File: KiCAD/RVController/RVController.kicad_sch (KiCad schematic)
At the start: 67 parts, among them IC1 MCP2561FD-E/P, J1 1727078, J2 1727078, J3 1727078, J4 1727078, J5 4-1437652-0, J6 Conn_01x02_Male, J7 Conn_01x02_Male, J8 54602-908LF, J9 54602-908LF, U1 FREESOC_MINI, U2 74HCT541, U3 VX7805-500, U4 H11L1SR2M, U5 H11L1SR2M, Y1 ECS-3961-240-AU-TR

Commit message: Almost done
Added mounting holes, labels, etc.
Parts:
- added H1, H2, H3, H4, H5, H6, H7, H8: MountingHole, MountingHole:MountingHole_3.2mm_M3_ISO14580, symbol Mechanical:MountingHole
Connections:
- net CAN_RX: now also U1.29 (15.5)
- net CAN_TX: now also U1.30 (15.4)
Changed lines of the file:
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@@
     (stroke (width 0) (type default) (color 0 0 0 0))
   )
+  (wire (pts (xy 66.04 68.58) (xy 77.47 68.58))
+    (stroke (width 0) (type default) (color 0 0 0 0))
+  )
   (wire (pts (xy 389.89 151.13) (xy 393.7 151.13))
     (stroke (width 0) (type default) (color 0 0 0 0))
@@
     (stroke (width 0) (type default) (color 0 0 0 0))
   )
+  (wire (pts (xy 66.04 71.12) (xy 77.47 71.12))
+    (stroke (width 0) (type default) (color 0 0 0 0))
+  )
   (wire (pts (xy 133.35 157.48) (xy 142.24 157.48))
     (stroke (width 0) (type default) (color 0 0 0 0))
@@
     (effects (font (size 1.27 1.27)) (justify left bottom))
   )
+  (label "CAN_RX" (at 77.47 71.12 0)
+    (effects (font (size 1.27 1.27)) (justify left bottom))
+  )
+  (label "CAN_TX" (at 77.47 68.58 0)
+    (effects (font (size 1.27 1.27)) (justify left bottom))
+  )
   (label "CAN_TX" (at 157.48 226.06 0)
     (effects (font (size 1.27 1.27)) (justify left bottom))
@@
     (pin "1")
   )
+  (symbol (lib_id "Mechanical:MountingHole") (at 335.28 250.19 0) (unit 1)
+    (in_bom no) (on_board yes) (fields_autoplaced)
+    (property "Reference" "H8" (id 0) (at 337.82 248.9199 0)
+      (effects (font (size 1.27 1.27)) (justify left))
+    )
+    (property "Value" "MountingHole" (id 1) (at 337.82 251.4599 0)
+      (effects (font (size 1.27 1.27)) (justify left))
+    )
+    (property "Footprint" "MountingHole:MountingHole_3.2mm_M3_ISO14580" (id 2) (at 335.28 250.19 0)
+      (effects (font (size 1.27 1.27)) hide)
+    )
+    (property "Datasheet" "~" (id 3) (at 335.28 250.19 0)
+      (effects (font (size 1.27 1.27)) hide)
+    )
+  )
   (symbol (lib_id "Device:R") (at 125.73 123.19 90) (unit 1)
     (in_bom yes) (on_board yes)
@@
     (pin "2")
   )
+  (symbol (lib_id "Mechanical:MountingHole") (at 335.28 240.03 0) (unit 1)
+    (in_bom no) (on_board yes) (fields_autoplaced)
+    (property "Reference" "H6" (id 0) (at 337.82 238.7599 0)
+      (effects (font (size 1.27 1.27)) (justify left))
+    )
+    (property "Value" "MountingHole" (id 1) (at 337.82 241.2999 0)
+      (effects (font (size 1.27 1.27)) (justify left))
+    )
+    (property "Footprint" "MountingHole:MountingHole_3.2mm_M3_ISO14580" (id 2) (at 335.28 240.03 0)
+      (effects (font (size 1.27 1.27)) hide)
+    )
+    (property "Datasheet" "~" (id 3) (at 335.28 240.03 0)
+      (effects (font (size 1.27 1.27)) hide)
+    )
+  )
   (symbol (lib_id "power:+5V_CAN") (at 210.82 207.01 0) (unit 1)
     (in_bom yes) (on_board yes) (fields_autoplaced)
@@
     (pin "2")
   )
+  (symbol (lib_id "Mechanical:MountingHole") (at 335.28 245.11 0) (unit 1)
+    (in_bom no) (on_board yes) (fields_autoplaced)
+    (property "Reference" "H7" (id 0) (at 337.82 243.8399 0)
+      (effects (font (size 1.27 1.27)) (justify left))
+    )
+    (property "Value" "MountingHole" (id 1) (at 337.82 246.3799 0)
+      (effects (font (size 1.27 1.27)) (justify left))
+    )
+    (property "Footprint" "MountingHole:MountingHole_3.2mm_M3_ISO14580" (id 2) (at 335.28 245.11 0)
+      (effects (font (size 1.27 1.27)) hide)
+    )
+    (property "Datasheet" "~" (id 3) (at 335.28 245.11 0)
+      (effects (font (size 1.27 1.27)) hide)
+    )
+  )
   (symbol (lib_id "Device:R") (at 59.69 153.67 0) (unit 1)
     (in_bom yes) (on_board yes)
@@
     (pin "C")
   )
+  (symbol (lib_id "Mechanical:MountingHole") (at 335.28 234.95 0) (unit 1)
+    (in_bom no) (on_board yes) (fields_autoplaced)
+    (property "Reference" "H5" (id 0) (at 337.82 233.6799 0)
+      (effects (font (size 1.27 1.27)) (justify left))
+    )
+    (property "Value" "MountingHole" (id 1) (at 337.82 236.2199 0)
+      (effects (font (size 1.27 1.27)) (justify left))
+    )
+    (property "Footprint" "MountingHole:MountingHole_3.2mm_M3_ISO14580" (id 2) (at 335.28 234.95 0)
+      (effects (font (size 1.27 1.27)) hide)
+    )
+    (property "Datasheet" "~" (id 3) (at 335.28 234.95 0)
+      (effects (font (size 1.27 1.27)) hide)
+    )
+  )
   (symbol (lib_id "power:GND") (at 33.02 91.44 0) (unit 1)
     (in_bom yes) (on_board yes) (fields_autoplaced)
@@
     (pin "C")
   )
+  (symbol (lib_id "Mechanical:MountingHole") (at 335.28 229.87 0) (unit 1)
+    (in_bom no) (on_board yes) (fields_autoplaced)
+    (property "Reference" "H4" (id 0) (at 337.82 228.5999 0)
+      (effects (font (size 1.27 1.27)) (justify left))
+    )
+    (property "Value" "MountingHole" (id 1) (at 337.82 231.1399 0)
+      (effects (font (size 1.27 1.27)) (justify left))
+    )
+    (property "Footprint" "MountingHole:MountingHole_3.2mm_M3_ISO14580" (id 2) (at 335.28 229.87 0)
+      (effects (font (size 1.27 1.27)) hide)
+    )
+    (property "Datasheet" "~" (id 3) (at 335.28 229.87 0)
+      (effects (font (size 1.27 1.27)) hide)
+    )
+  )
   (symbol (lib_id "Device:R") (at 59.69 186.69 0) (unit 1)
     (in_bom yes) (on_board yes)
@@
     (pin "1")
   )
+  (symbol (lib_id "Mechanical:MountingHole") (at 335.28 214.63 0) (unit 1)
+    (in_bom no) (on_board yes) (fields_autoplaced)
+    (property "Reference" "H1" (id 0) (at 337.82 213.3599 0)
+      (effects (font (size 1.27 1.27)) (justify left))
+    )
+    (property "Value" "MountingHole" (id 1) (at 337.82 215.8999 0)
+      (effects (font (size 1.27 1.27)) (justify left))
+    )
+    (property "Footprint" "MountingHole:MountingHole_3.2mm_M3_ISO14580" (id 2) (at 335.28 214.63 0)
+      (effects (font (size 1.27 1.27)) hide)
+    )
+    (property "Datasheet" "~" (id 3) (at 335.28 214.63 0)
+      (effects (font (size 1.27 1.27)) hide)
+    )
+  )
   (symbol (lib_id "power:+5V") (at 66.04 43.18 0) (unit 1)
     (in_bom yes) (on_board yes) (fields_autoplaced)
@@
     (pin "1")
   )
+  (symbol (lib_id "Mechanical:MountingHole") (at 335.28 219.71 0) (unit 1)
+    (in_bom no) (on_board yes) (fields_autoplaced)
+    (property "Reference" "H2" (id 0) (at 337.82 218.4399 0)
+      (effects (font (size 1.27 1.27)) (justify left))
+    )
+    (property "Value" "MountingHole" (id 1) (at 337.82 220.9799 0)
+      (effects (font (size 1.27 1.27)) (justify left))
+    )
+    (property "Footprint" "MountingHole:MountingHole_3.2mm_M3_ISO14580" (id 2) (at 335.28 219.71 0)
+      (effects (font (size 1.27 1.27)) hide)
+    )
+    (property "Datasheet" "~" (id 3) (at 335.28 219.71 0)
+      (effects (font (size 1.27 1.27)) hide)
+    )
+  )
   (symbol (lib_id "power:GND_CAN") (at 218.44 271.78 0) (unit 1)
     (in_bom yes) (on_board yes) (fields_autoplaced)
@@
     (pin "1")
   )
+  (symbol (lib_id "Mechanical:MountingHole") (at 335.28 224.79 0) (unit 1)
+    (in_bom no) (on_board yes) (fields_autoplaced)
+    (property "Reference" "H3" (id 0) (at 337.82 223.5199 0)
+      (effects (font (size 1.27 1.27)) (justify left))
+    )
+    (property "Value" "MountingHole" (id 1) (at 337.82 226.0599 0)
+      (effects (font (size 1.27 1.27)) (justify left))
+    )
+    (property "Footprint" "MountingHole:MountingHole_3.2mm_M3_ISO14580" (id 2) (at 335.28 224.79 0)
+      (effects (font (size 1.27 1.27)) hide)
+    )
+    (property "Datasheet" "~" (id 3) (at 335.28 224.79 0)
+      (effects (font (size 1.27 1.27)) hide)
+    )
+  )
   (symbol (lib_id "Schematic:SS16MH") (at 247.65 110.49 90) (unit 1)
     (in_bom yes) (on_board yes) (fields_autoplaced)
@@
       (reference "D26") (unit 1) (value "ATV02W240B") (footprint "Footprints:SODFL2512X73N")
     )
+    (path "/c704bbfb-71ae-4908-a3cf-bc2bd43df023"
+      (reference "H1") (unit 1) (value "MountingHole") (footprint "MountingHole:MountingHole_3.2mm_M3_ISO14580")
+    )
+    (path "/de77b565-8d7d-4e6e-8ab1-bcd72032f282"
+      (reference "H2") (unit 1) (value "MountingHole") (footprint "MountingHole:MountingHole_3.2mm_M3_ISO14580")
+    )
+    (path "/e980f142-5464-462f-987b-1671d88515a0"
+      (reference "H3") (unit 1) (value "MountingHole") (footprint "MountingHole:MountingHole_3.2mm_M3_ISO14580")
+    )
+    (path "/bfa32192-5b21-496a-9b92-6fdd025d263e"
+      (reference "H4") (unit 1) (value "MountingHole") (footprint "MountingHole:MountingHole_3.2mm_M3_ISO14580")
+    )
+    (path "/684fccac-62c3-4aa7-b45b-93649e0e524d"
+      (reference "H5") (unit 1) (value "MountingHole") (footprint "MountingHole:MountingHole_3.2mm_M3_ISO14580")
+    )
+    (path "/55708a54-043a-40dd-a394-e39898b05970"
+      (reference "H6") (unit 1) (value "MountingHole") (footprint "MountingHole:MountingHole_3.2mm_M3_ISO14580")
+    )
+    (path "/5d658465-34e3-47c9-8c1c-64276b8eda22"
+      (reference "H7") (unit 1) (value "MountingHole") (footprint "MountingHole:MountingHole_3.2mm_M3_ISO14580")
+    )
+    (path "/34b1f6de-8080-4231-916b-2ce7a1c2638e"
+      (reference "H8") (unit 1) (value "MountingHole") (footprint "MountingHole:MountingHole_3.2mm_M3_ISO14580")
+    )
     (path "/dbe415dc-83a6-4820-a16b-1dc1bf799f8a"

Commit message: Done?
Routed, etc. Exported STEP.
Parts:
- removed H8: MountingHole, MountingHole:MountingHole_3.2mm_M3_ISO14580, symbol Mechanical:MountingHole
- added C8: 4700pF, Capacitor_SMD:C_0603_1608Metric, symbol Device:C
- added J10, J11: Conn_01x02_Male, Connector_PinHeader_2.54mm:PinHeader_1x02_P2.54mm_Vertical, symbol Connector:Conn_01x02_Male
- added J12: 284392-2, Footprints:TE_284392-2, symbol Schematic:284392-2
- added R23: 300R, Resistor_SMD:R_0805_2012Metric, symbol Device:R
- added R24, R29: 60R, Resistor_SMD:R_0805_2012Metric, symbol Device:R
- J1, J3, J4: footprint PHOENIX_1727078 -> Footprints:PHOENIX_1727078
- J2: footprint PHOENIX_1727078 -> Footprints:PHOENIX_1727078; PN (none) -> 1727078
- J5: footprint TE_4-1437652-0 -> Footprints:TE_4-1437652-0
- R17, R22: value 330R -> 300R; PN RMCF0805JT330R -> RMCF0805JT300R
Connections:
- net +5V_CAN: now also J12.1
- net CANH: now also J10.1 (Pin_1)
- net CANL: now also J11.1 (Pin_1)
- net at IC1.5 (SPLIT): now also R23.1
- net GNDPWR renamed GND_CAN
- net GND_CAN: now also C8.2, J12.2
- new net: C8.1, R23.2, R24.2, R29.1
- new net: J11.2 (Pin_2), R29.2
- new net: J10.2 (Pin_2), R24.1
- no-connect marks 0 -> 25
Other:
- moved on the sheet: C6

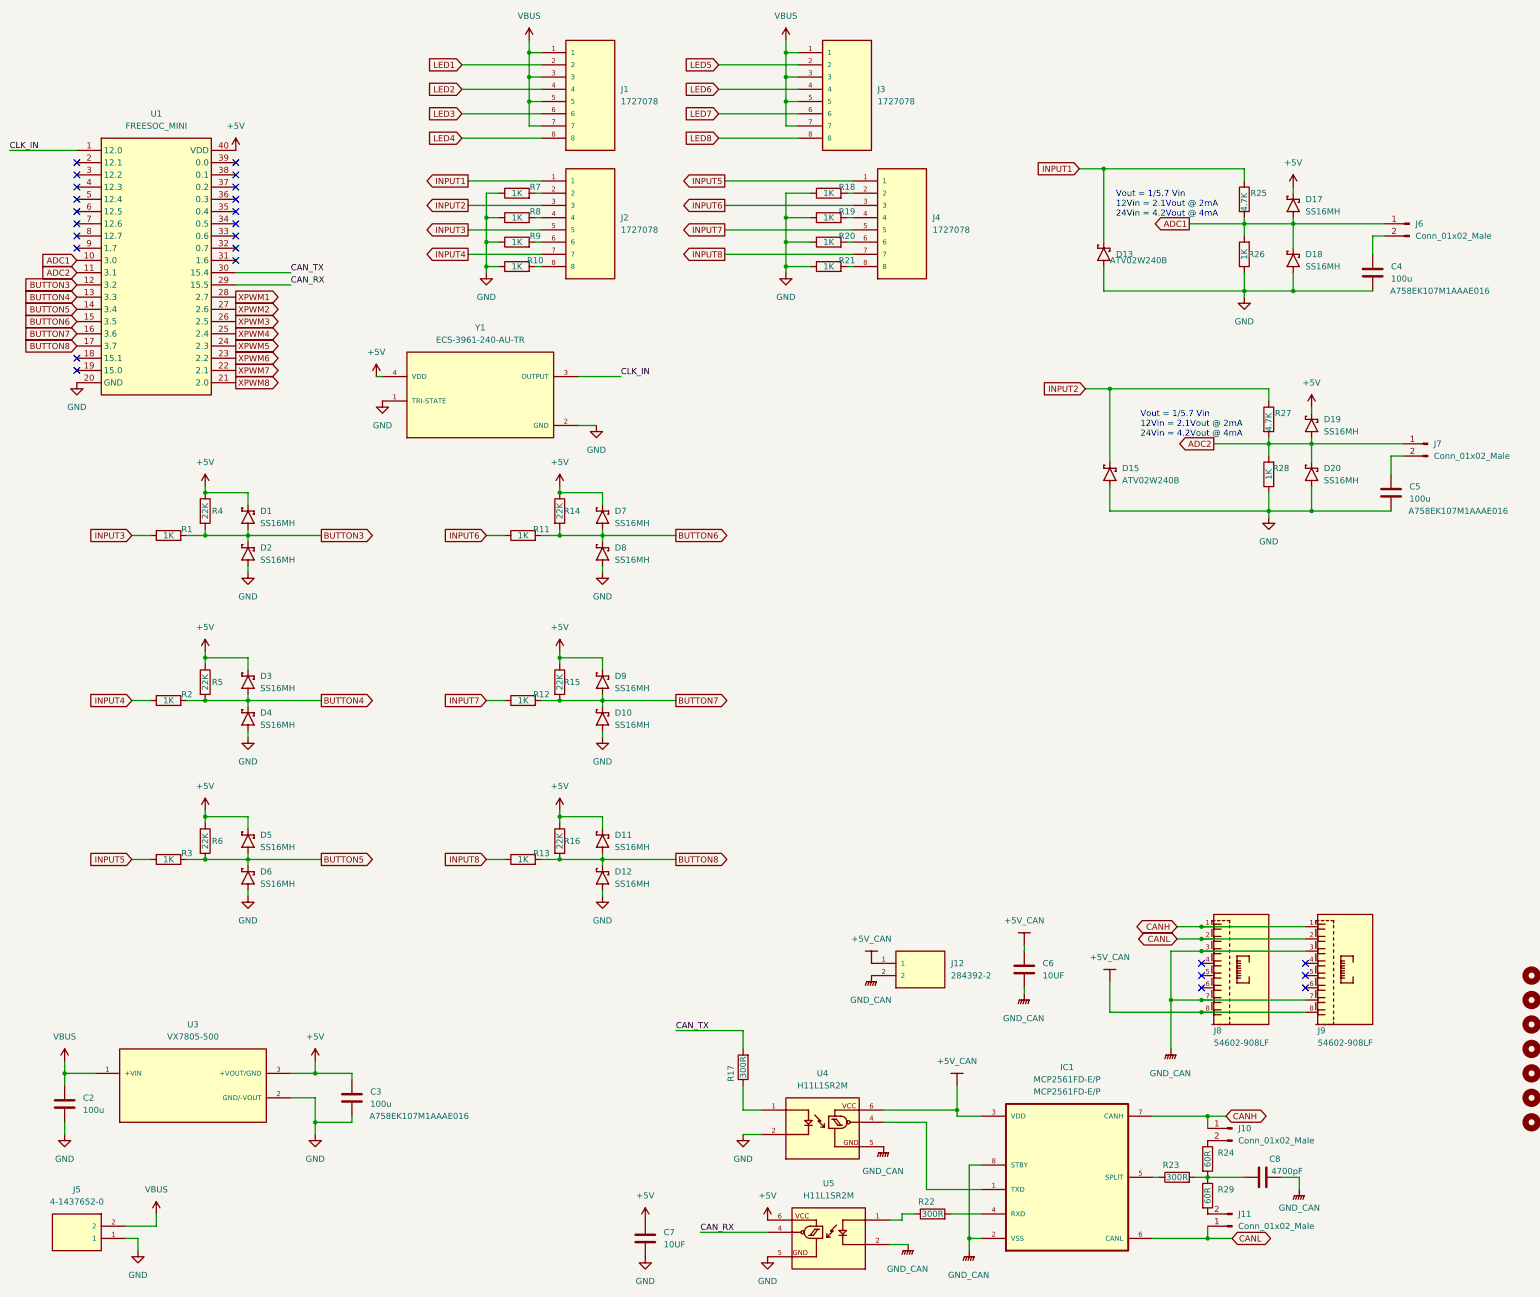
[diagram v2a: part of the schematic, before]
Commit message: Updated to SMD socket
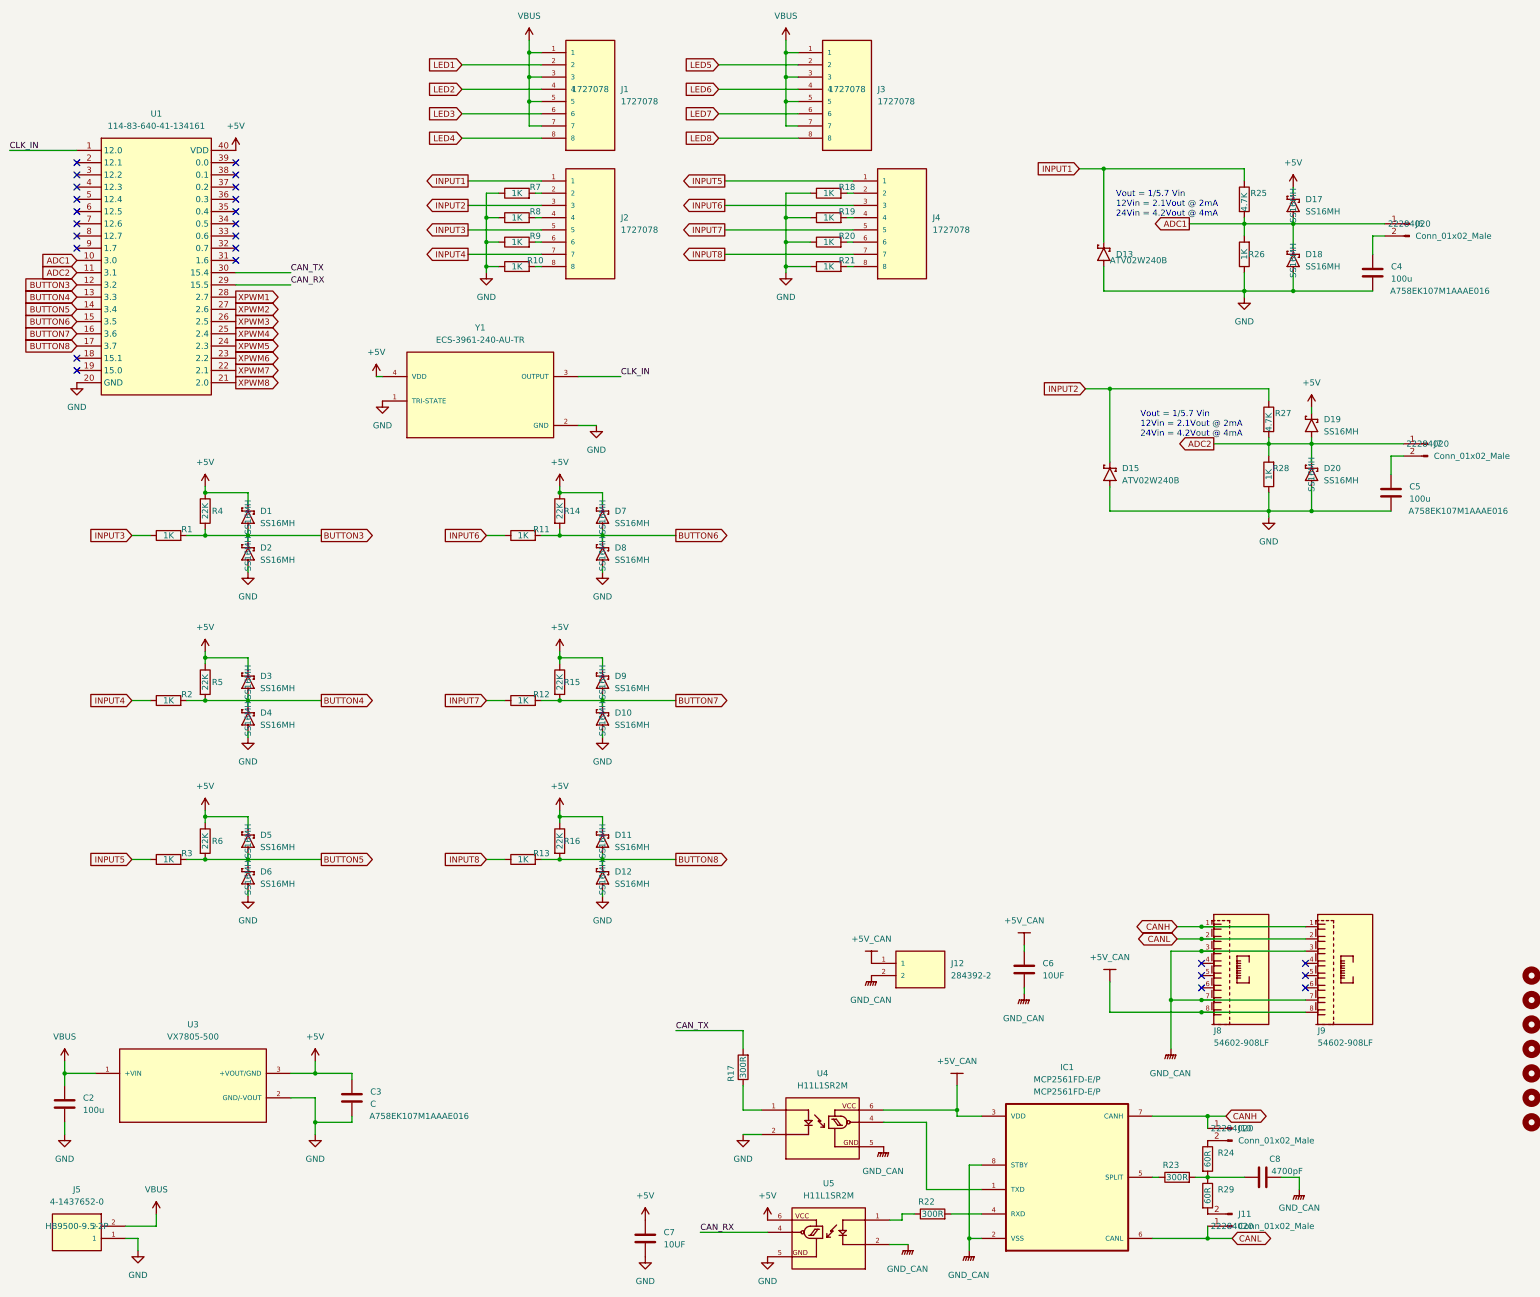
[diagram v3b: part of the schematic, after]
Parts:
- C2: PN (none) -> EEH-AZF1V101B; Part Number EEH-AZF1V101B -> (none)
- C3: value 100u -> C; PN (none) -> A758EK107M1AAAE016
- C4, C5: PN (none) -> A758EK107M1AAAE016; Part Number A758EK107M1AAAE016 -> (none)
- D1, D10, D11, D12, D17, D18, D2, D20, D3, D4, D5, D6, D7, D8, D9: PN (none) -> SS16MH
- J1, J3: footprint Footprints:PHOENIX_1727078 -> PHOENIX_1727078; PN (none) -> 1727078
- J10, J11, J6, J7: PN (none) -> 22284020
- J12: PN (none) -> 284392-2
- J2, J4: footprint Footprints:PHOENIX_1727078 -> PHOENIX_1727078
- J5: footprint Footprints:TE_4-1437652-0 -> TE_4-1437652-0; PN (none) -> HB9500-9.5-2P
- J8, J9: PN (none) -> 54602-908LF
- U1: value FREESOC_MINI -> 114-83-640-41-134161; footprint Package_DIP:DIP-40_W15.24mm_Socket_LongPads -> Footprints:114-83-640-41-134161; PN (none) -> 114-83-640-41-134161
- U3: PN (none) -> VX7805-500
- U4, U5: PN (none) -> H11L1SR2M
- Y1: PN (none) -> ECS-3961-240-AU-TR
